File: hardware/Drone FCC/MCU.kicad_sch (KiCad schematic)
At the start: 34 parts, among them SW1 SW_MEC_5E, Y1 12MHz, Y2 32.768kHz

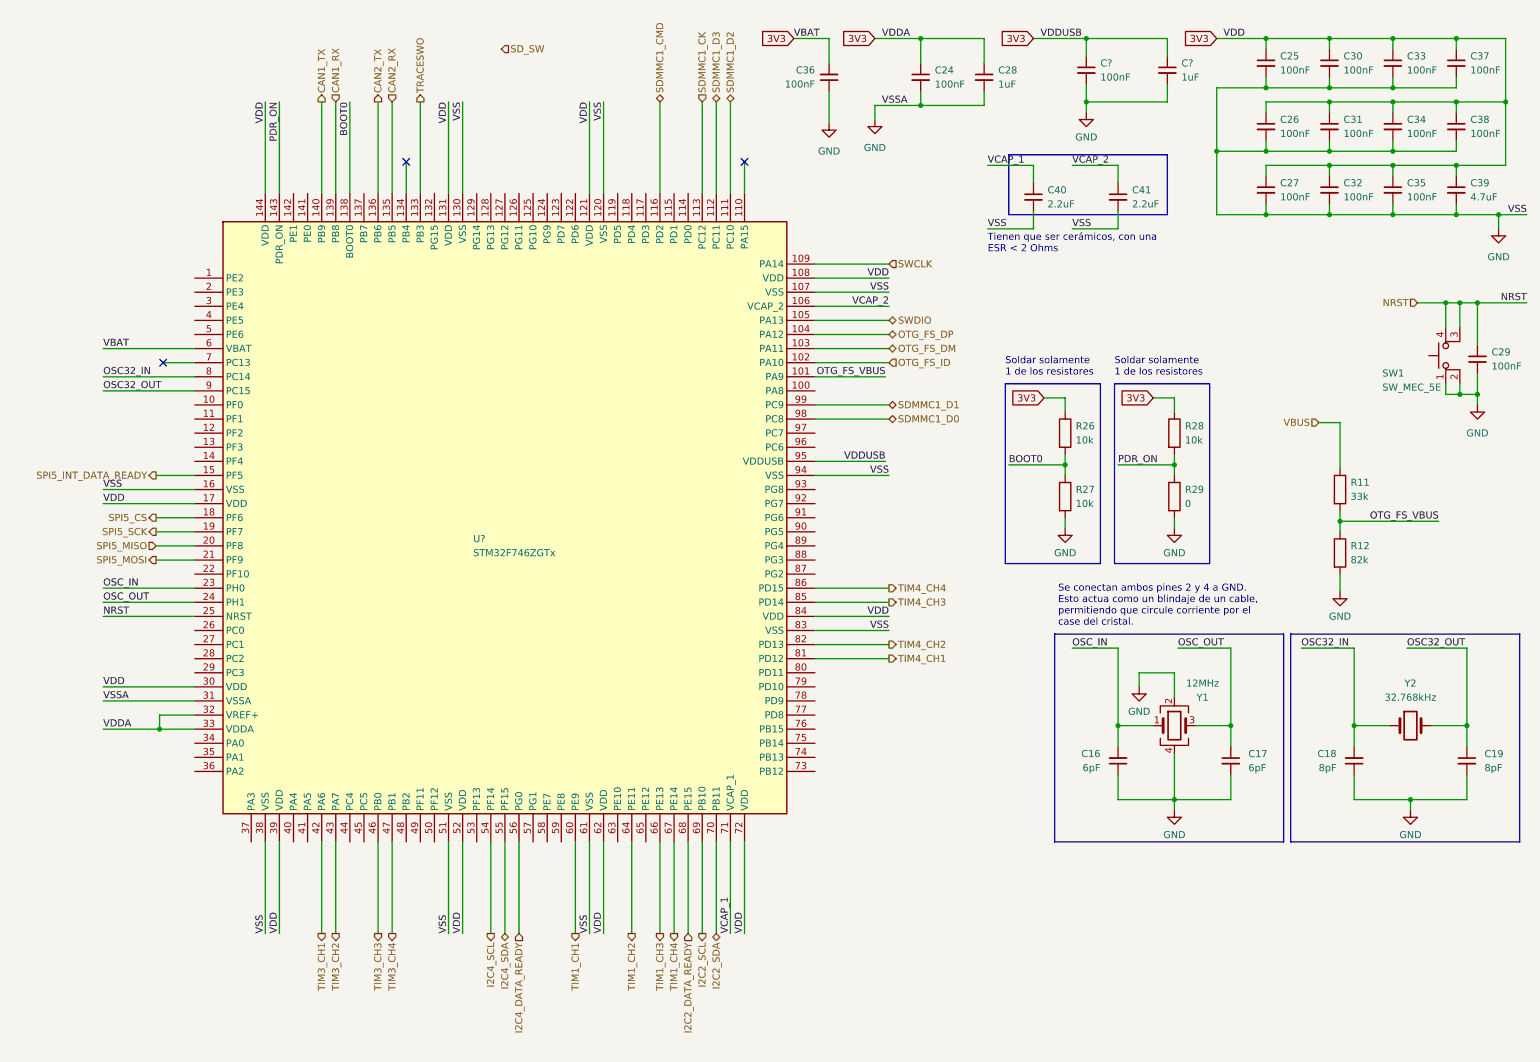
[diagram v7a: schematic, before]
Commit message: add external communication connectors
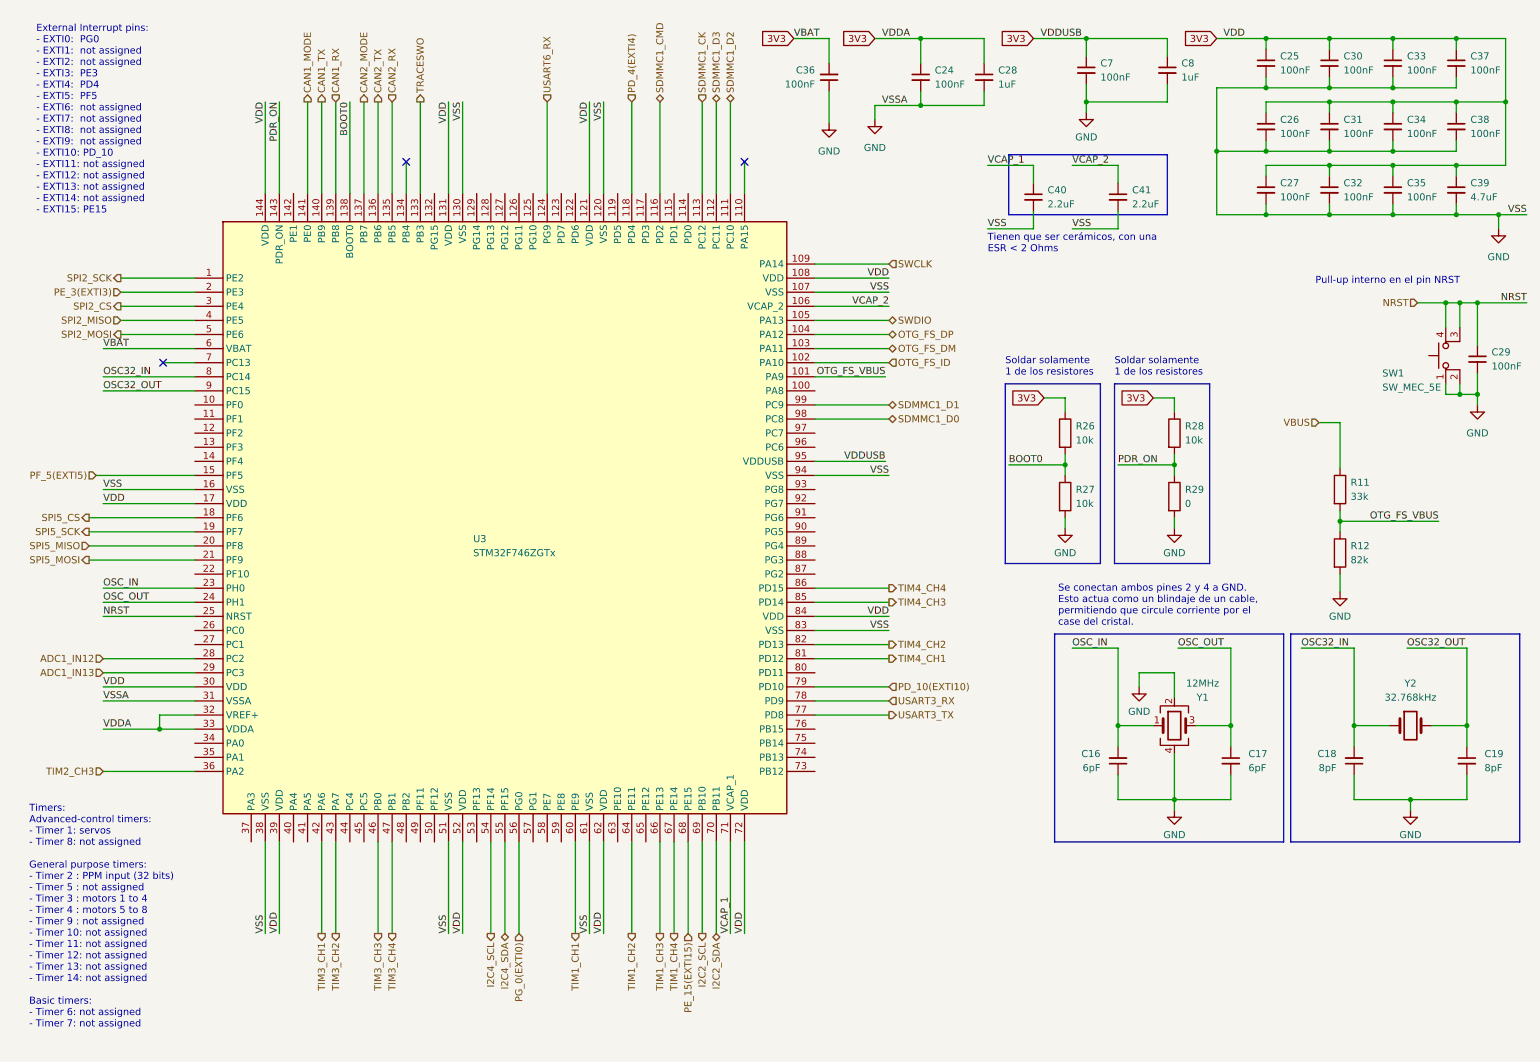
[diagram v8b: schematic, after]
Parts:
- gave numbers to parts that had none: 3
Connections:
- net SPI2_SCK: now reaches U3.1 (PE2)
- net PD_4(EXTI4): now reaches U3.118 (PD4)
- net USART6_RX: now reaches U3.124 (PG9)
- net CAN2_MODE: now reaches U3.137 (PB7)
- net CAN1_MODE: now reaches U3.141 (PE0)
- net PE_3(EXTI3): now reaches U3.2 (PE3)
- net ADC1_IN12: now reaches U3.28 (PC2)
- net ADC1_IN13: now reaches U3.29 (PC3)
- net SPI2_CS: now reaches U3.3 (PE4)
- net TIM2_CH3: now reaches U3.36 (PA2)
- net SPI2_MISO: now reaches U3.4 (PE5)
- net SPI2_MOSI: now reaches U3.5 (PE6)
- net USART3_TX: now reaches U3.77 (PD8)
- net USART3_RX: now reaches U3.78 (PD9)
- net PD_10(EXTI10): now reaches U3.79 (PD10)
- net I2C2_DATA_READY renamed PE_15(EXTI15)
- net I2C4_DATA_READY renamed PG_0(EXTI0)
- net SPI5_INT_DATA_READY renamed PF_5(EXTI5)
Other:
- note added: "External Interrupt pins: - EXTI0: PG0 - EXTI1: not assigned - EXTI2: not assigned - EXTI3: PE3 - EXTI4: PD4 - EXTI5: PF5 - EXTI6: not assigned - EXTI7: not assigned - EXTI8: not assigned - EXTI9: not assigned - EXTI10: PD_10 - EXTI11: not assigned - EXTI12: not assigned - EXTI13: not assigned - EXTI14: not assigned - EXTI15: PE15"
- note added: "Pull-up interno en el pin NRST"
- note added: "Timers: Advanced-control timers: - Timer 1: servos - Timer 8: not assigned General purpose timers: - Timer 2 : PPM input (32 bits) - Timer 5 : not assigned - Timer 3 : motors 1 to 4 - Timer 4 : motors 5 to 8 - Timer 9 : not assigned - Timer 10: not assigned - Timer 11: not assigned - Timer 12: not assigned - Timer 13: not assigned - Timer 14: not assigned Basic timers: - Timer 6: not assigned - T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"
